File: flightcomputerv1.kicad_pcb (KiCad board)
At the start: 4 copper layers, 120 x 68 mm, 51 parts, among them IC1 MMC5983MA, J1 Screw_Terminal_01x02, J2 Screw_Terminal_01x02, J5 Conn_01x02, J6 Conn_01x24, J7 Conn_01x24, J8 Conn_Coaxial, J9 Conn_Coaxial, M1 Motor_Servo, M2 Motor_Servo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

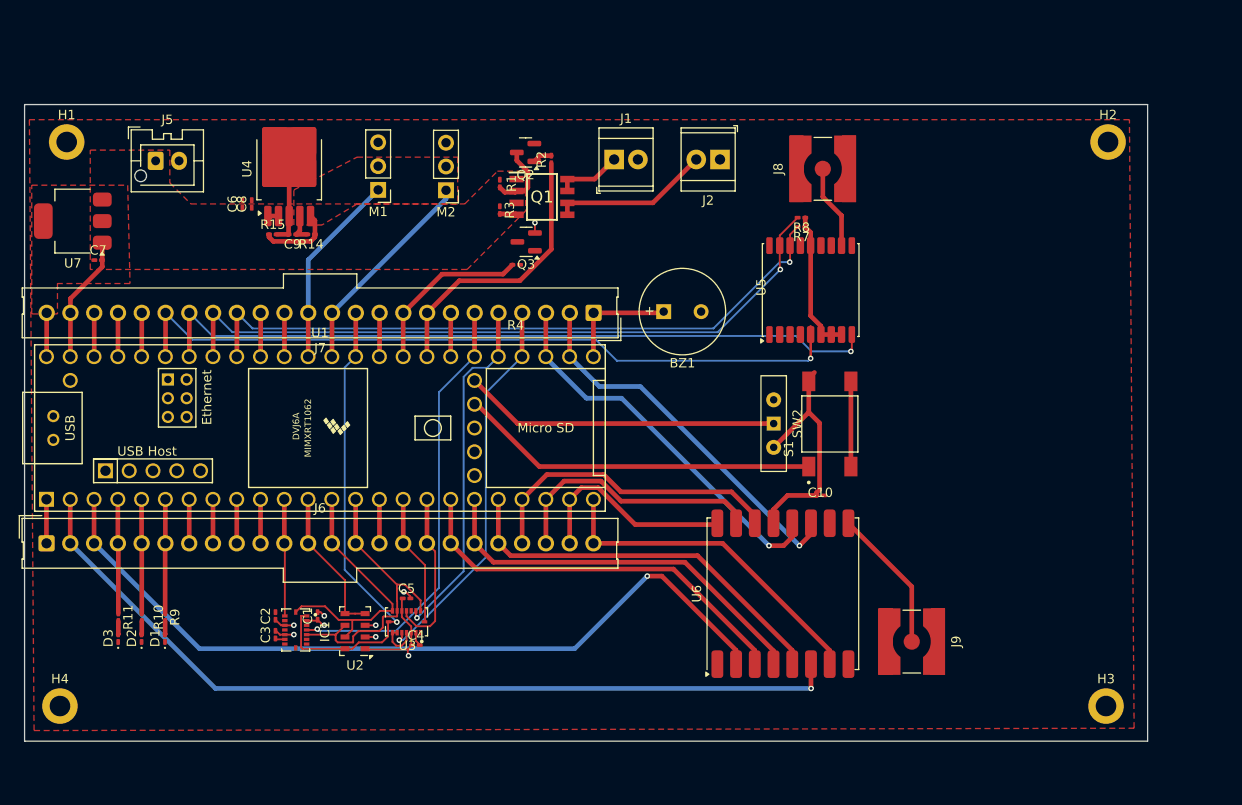
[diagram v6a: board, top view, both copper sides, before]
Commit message: moved buttons
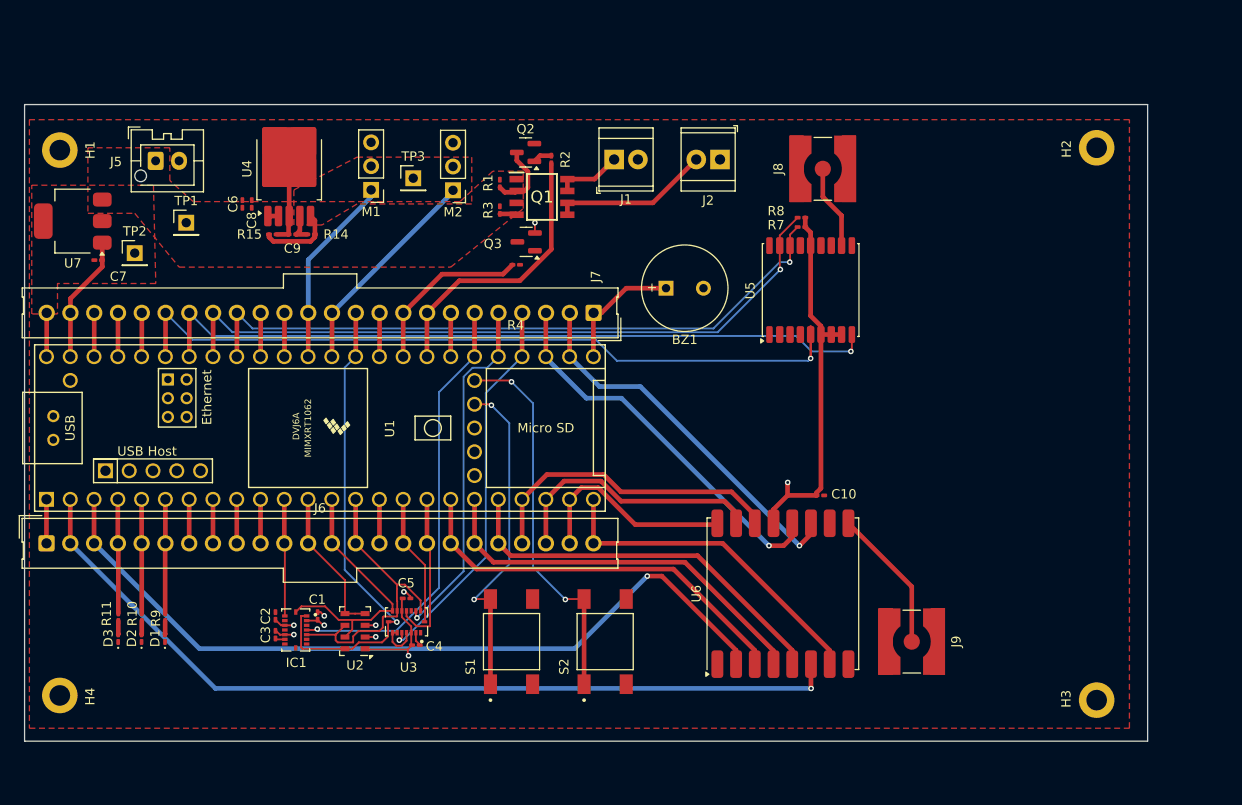
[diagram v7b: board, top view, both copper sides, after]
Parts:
- removed SW2: SW_Wuerth_450301014042, Button_Switch_THT:SW_Slide-03_Wuerth-WS-SLTV_10x2.5x6.4_P2.54mm
- added S2: TS04-66-70-BK-160-SMT, HPRfootprints:SW_TS04-66-70-BK-160-SMT, F.Cu at (112.0, 115.5)
- added TP1: TestPoint, Connector_PinHeader_2.54mm:PinHeader_1x01_P2.54mm_Vertical, F.Cu at (67.2, 70.8)
- added TP2: TestPoint, Connector_PinHeader_2.54mm:PinHeader_1x01_P2.54mm_Vertical, F.Cu at (61.8, 74.0)
- added TP3: TestPoint, Connector_PinHeader_2.54mm:PinHeader_1x01_P2.54mm_Vertical, F.Cu at (91.5, 66.0)
- moved S1 41.2 mm to (102.0, 115.5)
- moved BZ1 2.51 mm to (118.5, 77.8)
- moved H2 1.37 mm to (164.5, 62.8)
- moved H3 1.18 mm to (164.5, 121.8)
- moved H1 1.14 mm to (53.8, 63.0)
- moved H4 1.13 mm to (53.8, 121.2)
- moved M1 0.75 mm to (87.0, 67.2)
- moved M2 0.75 mm to (95.8, 67.3)
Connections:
- S1 pad 3: /teensy_3.3v -> Net-(U1-PROGRAM)
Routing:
- net GND: track 55.6 -> 46.5 mm
- net /teensy_onoff: track 33.9 -> 40.8 mm, vias 0 -> 2
- net Net-(U1-PROGRAM): track 38.5 -> 35.8 mm, vias 0 -> 2
- net /buzz_pwm: track 12.2 -> 13.5 mm
- net /teensy_3.3v: track 67.0 -> 66.5 mm, vias 3 -> 4

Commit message: magnetometer had wrong footprint. fixed all DRC errors. need to remake gerber
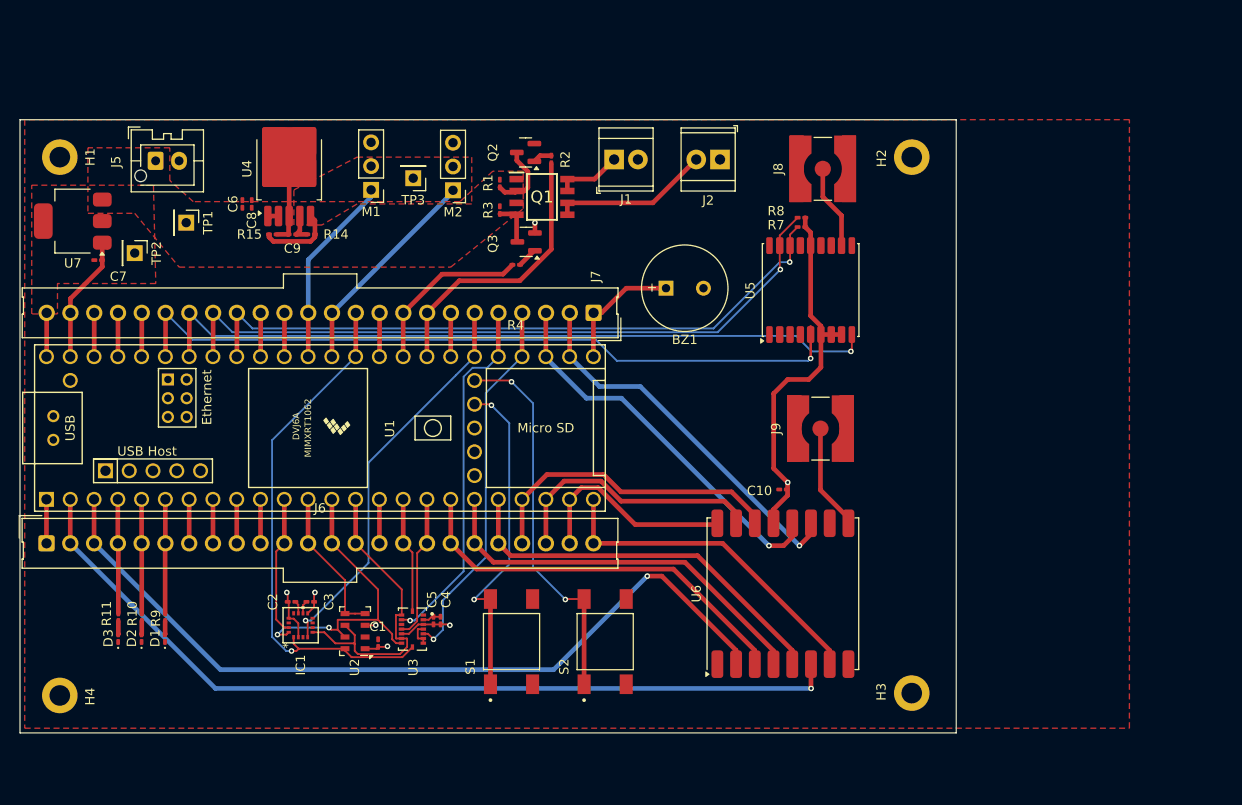
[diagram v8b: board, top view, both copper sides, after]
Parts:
- IC1: footprint HPRfootprints:PQFN50P450X300X100-16N -> HPRfootprints:MMC5983MA_MEM
- moved J9 24.8 mm to (135.0, 92.8), turned to 90 degrees
- moved H2 19.8 mm to (144.8, 63.8)
- moved H3 19.8 mm to (144.8, 121.0)
- moved C1 7.09 mm to (87.8, 115.7)
- moved C3 5.11 mm to (80.5, 111.2), turned to 0 degrees
- moved C10 4.03 mm to (131.0, 99.2), turned to 180 degrees
- moved C5 3.73 mm to (93.7, 113.2), turned to 90 degrees
- moved C4 3.72 mm to (94.4, 113.2), turned to 90 degrees
- moved C2 2.28 mm to (78.5, 111.2), turned to 0 degrees
- moved U3 1.00 mm to (91.4, 114.2), turned to -90 degrees
- moved H1 0.75 mm to (53.8, 63.8)
- moved IC1 0.73 mm to (79.5, 113.8), turned to 90 degrees
- turned TP1 to -90 degrees
- turned TP2 to -90 degrees
- turned TP3 to 180 degrees
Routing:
- net /SENSE_mosi: track 28.3 -> 33.4 mm, vias 0 -> 2
- net /mag_cs: track 47.1 -> 42.6 mm
- net /SENSE_sck: track 52.1 -> 56.4 mm
- net Net-(J9-In): track 15.4 -> 11.3 mm
- net Net-(Q1-G2): track 1.83 -> 4.76 mm
- net /teensy_3.3v: track 66.5 -> 63.7 mm
- net /mag_int: track 12.5 -> 15.0 mm
- net GND: track 46.5 -> 44.1 mm, vias 6 -> 3
- net Net-(Q3-B): track 0.00 -> 2.21 mm
- net /radio_miso: track 86.1 -> 88.0 mm
- net /imu_gyro_cs: track 41.5 -> 40.1 mm
- net /imu_gyro_int1: track 17.2 -> 15.9 mm
- net /SENSE_miso: track 32.6 -> 33.8 mm
- net /imu_accel_cs: track 37.9 -> 38.9 mm
- net /imu_accel_int1: track 14.1 -> 13.3 mm
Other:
- board size 120 x 68 mm -> 100 x 65.5 mm
